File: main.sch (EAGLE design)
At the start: 4 parts

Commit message: Added initial components
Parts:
- added C1: 100n, resistor:C-EUC0805
- added C12, C2, C3, C4, C56, C62: 100nF, resistor:C-EUC0805
- added C5, C58, C61: 1uF_X5R, resistor:C-EUC0805
- added C57: 10nF X7R, resistor:C-EUC0805
- added C59, C60: 10uF, resistor:CPOL-EUSMCC
- added D1: BAT54S, diode:BAT54S
- added D14: BAT60JFILM, diode:DIODE-SOD323-W
- added IC17: LD398533RM, st-microelectronics:LD398533RM
- added IC18: LD1117S50TR, v-reg:LD117AS50TR
- added J1: DCJ0202, con-jack:DCJ0202
- added LED1, LED14: ROOD, led:LEDCHIP-LED0805
- added R1: 10K, resistor:R-EU_R0805
- added R2, R39, R6, R7, R8: 1K, resistor:R-EU_R0805
- added R3, R4, R5: 4K7, resistor:R-EU_R0805
- added S1: (no value), switch-omron:10-XX
- added U1: TMP275AIDR, TMP275AIDR:TMP275AIDR
- added U4: ESP-WROOM-32, esp32:ESP-WROOM-32
- added X1: 1751251, con-phoenix-350:1751251
- added X2: 87438-02, con-molex:87438-02
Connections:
- new net +12V: C59.+, IC18.IN, J1.1, X2-2.S
- new net +3V3: C12.1, C4.1, C5.1, C61.1, C62.1, D1.C2, IC17.VO, R1.2, R3.2, R4.2, R5.2, R7.2, R8.2, U1.V+, U4.3V3
- new net +5V: C60.+, D14.A, IC18.OUT, R39.2
- new net BTN: C2.1, R8.1, S1.S1
- new net GND: C1.2, C12.2, C2.2, C3.2, C4.2, C5.2, C56.2, C57.2, C58.2, C59.-, C60.-, C61.2, C62.2, D1.A1, IC17.GND, IC18.ADJ, J1.3, LED1.C, LED14.C, S1.P, U1.A0, U1.A1, U1.A2, U1.GND, U4.GND@1, U4.GND@15, U4.GND@38, X2-1.S
- new net I2C_SCL: R3.1, U1.SCL
- new net I2C_SDA: R4.1, U1.SDA
- new net LED: R6.2
- new net N$1: C1.1, D1.C1A2, R1.1, R2.2
- new net N$102: C57.1, IC17.BYPASS
- new net N$113: C56.1, C58.1, D14.C, IC17.VIN, IC17.VINH
- new net N$2: R2.1
- new net N$5: LED1.A, R6.1
- new net N$6: C3.1, R7.1, U4.EN
- new net N$99: LED14.A, R39.1
- new net RDX0: U4.RXD0
- new net TEMP_ALERT: R5.1, U1.ALERT
- new net TXD0: U4.TXD0

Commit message: Update :)
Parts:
- added C10, C7, C9: 100n, resistor:C-EUC0805
- added C6, C8: 10nF X7R, resistor:C-EUC0805
- added D2: BAT54S, diode:BAT54S
- added D3: BAT60JFILM, diode:DIODE-SOD323-W
- added IC1, IC2: PM8834-SO08N, PM8834:PM8834-SO08N
- added JP1: (no value), pinhead:PINHD-1X6
- added Q1, Q2, Q3, Q4: IRF3205SPBF, IRF3205SPBF:IRF3205SPBF
- added R10: 1K, resistor:R-EU_R0805
- added R11, R12, R13, R14, R9: 10K, resistor:R-EU_R0805
- added X3: 1751251, con-phoenix-350:1751251
- added X4: 1751277, con-phoenix-350:1751277
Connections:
- net N$1 renamed INP2
- new net CTS: JP1.6
- new net INP1: C10.1, D2.C1A2, R10.2, R9.1
- new net N$1: R11.2
- new net N$10: IC1.EN1, IC2.EN1, R11.1, R13.1
- new net N$12: IC1.OUT1, Q2.G
- new net N$13: IC1.OUT2, Q1.G
- new net N$14: Q2.D, X4-3.K
- new net N$15: IC2.OUT1, Q4.G
- new net N$16: IC2.OUT2, Q3.G
- new net N$17: Q3.D, X4-4.K
- new net N$18: Q4.D, X4-5.K
- new net N$19: R12.2
- new net N$20: R10.1, X3-2.K
- new net N$22: X3-1.K
- new net N$23: R14.2
- new net N$24: R13.2
- new net N$4: X1-1.K
- new net N$7: Q1.D, X4-2.K
- new net N$9: IC1.IN2, IC2.IN2
- new net PWM1: IC1.IN1
- new net PWM2: IC1.EN2, R12.1
- new net PWM3: IC2.IN1
- new net PWM4: IC2.EN2, R14.1
- new net RTS: JP1.5
- new net UART_5V: D3.A, JP1.1
- net +12V: now also C6.1, C7.1, C8.1, C9.1, IC1.VCC, IC2.VCC, X4-1.K
- net +3V3: now also D2.C2, R9.2
- net GND: now also C10.2, C6.2, C7.2, C8.2, C9.2, D2.A1, IC1.GND, IC2.GND, JP1.2, Q1.S, Q2.S, Q3.S, Q4.S, X1-3.K, X3-3.K
- net N$113: now also D3.C
- net N$2: now also X1-2.K
- net RDX0: now also JP1.4
- net TXD0: now also JP1.3
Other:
- note added: "RXD"
- note added: "TXD"

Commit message: layouting
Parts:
- removed X2: 87438-02, con-molex:87438-02
- added D4: TSOP57238TT1, SparkFun-Sensors:TSOP57238TT1
- added R15, R16: 1K, resistor:R-EU_R0805
- added U2: SI7021, SparkFun-Sensors:SI7021
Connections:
- removed net PWM4: IC2.EN2, R14.1
- new net PWM0: IC1.IN1, U4.IO18
- net +12V: no longer X2-2.S
- net GND: now also R15.1, R16.1; no longer X2-1.S
- net N$2: now also R15.2
- net N$20: now also R16.2
- net PWM1: now also IC1.EN2, R12.1, U4.IO19; no longer IC1.IN1
- net PWM2: now also IC2.IN1, U4.IO22; no longer IC1.EN2, R12.1
- net PWM3: now also IC2.EN2, R14.1, U4.IO23; no longer IC2.IN1
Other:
- moved on the sheet: X1-1, X1-2, X1-3, X3-1, X3-2, X3-3

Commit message: added level shifters
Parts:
- removed J1: DCJ0202, con-jack:DCJ0202
- added JP2: (no value), pinhead:PINHD-1X4
- added JP3, JP4, JP6: (no value), adafruit:PINHD-1X3
- added Q5, Q6, Q7, Q8: BSS138, SparkFun:MOSFET-NCHANNELSMD
- added R17, R18: 1K, resistor:R-EU_R0805
- added R19, R20, R21, R22, R23, R24, R25, R26, R27, R28, R29, R30: 10K, resistor:R-EU_R0805
- added X2: 1751248, con-phoenix-350:1751248
- JP1: device pinhead:PINHD-1X6 -> adafruit:PINHD-1X3
- R10, R2: value 1K -> 10R
- R15, R16: value 1K -> X
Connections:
- removed net CTS: JP1.6
- removed net N$1: R11.2
- removed net N$19: R12.2
- removed net N$23: R14.2
- removed net N$24: R13.2
- removed net RTS: JP1.5
- new net HV: JP1.1, JP3.1, JP4.1, JP6.1, R24.1, R26.1, R28.1, R30.1
- new net HV1: JP6.2, Q5.D, R24.2
- new net HV2: JP1.2, Q6.D, R26.2
- new net HV3: JP3.2, Q7.D, R28.2
- new net HV4: JP4.2, Q8.D, R30.2
- new net LV0: Q5.S, R23.2
- new net LV1: Q6.S, R25.2
- new net LV2: Q7.S, R27.2
- new net LV3: Q8.S, R29.2
- new net N$2001: IC2.IN2, R14.1
- new net N$2OO: IC2.EN1, R13.1
- new net N$3: D2.C1A2, R10.2, R17.1
- new net N$8: D1.C1A2, R18.1, R2.2
- net +12V: now also R11.2, R12.2, X2-1.K; no longer J1.1
- net +3V3: now also Q5.G, Q6.G, Q7.G, Q8.G, R23.1, R25.1, R27.1, R29.1
- net BTN: now also U4.IO34
- net GND: now also JP1.3, JP2.2, JP3.3, JP4.3, JP6.3, R13.2, R14.2, R19.2, R20.2, R21.2, R22.2, X2-2.K; no longer J1.3, JP1.2
- net I2C_SCL: now also R4.1, U4.IO22; no longer R3.1
- net I2C_SDA: now also R3.1, U4.IO23; no longer R4.1
- net INP1: now also R17.2, U4.IO25; no longer D2.C1A2, R10.2
- net INP2: now also R18.2, U4.IO33; no longer D1.C1A2, R2.2
- net LED: now also U4.IO32
- net N$10: no longer IC2.EN1, R13.1
- net N$9: now also R12.1; no longer IC2.IN2
- net PWM0: now also R22.1, U4.IO17; no longer U4.IO18
- net PWM1: now also R21.1, U4.IO5; no longer R12.1, U4.IO19
- net PWM2: now also R20.1, U4.IO18; no longer U4.IO22
- net PWM3: now also R19.1, U4.IO19; no longer R14.1, U4.IO23
- net RDX0: now also JP2.4; no longer JP1.4
- net TEMP_ALERT: now also U4.IO21
- net TXD0: now also JP2.3; no longer JP1.3
- net UART_5V: now also JP2.1; no longer JP1.1
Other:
- moved on the sheet: C1, C10, C8, C9, IC1, IC2, Q1, Q2, Q3, Q4, R1, R11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

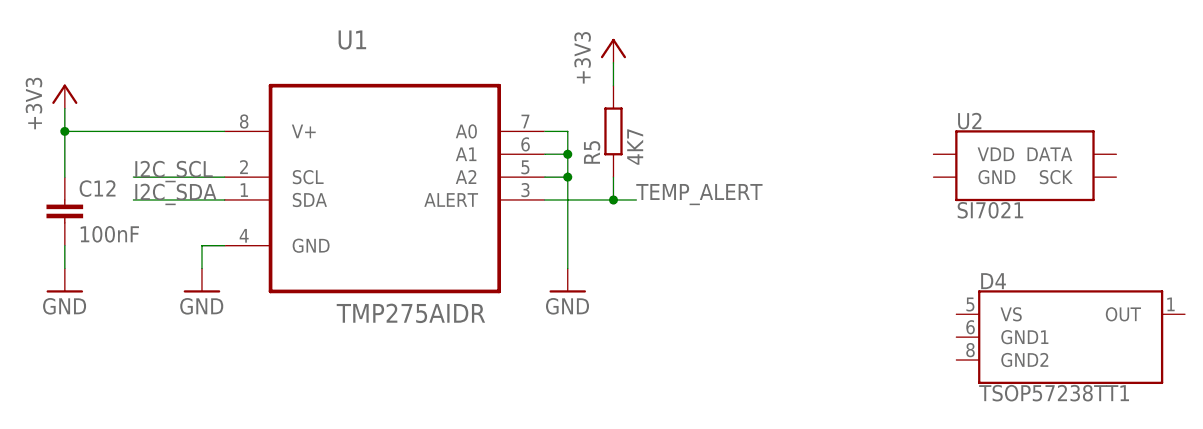
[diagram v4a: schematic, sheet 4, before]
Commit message: Removed sensors
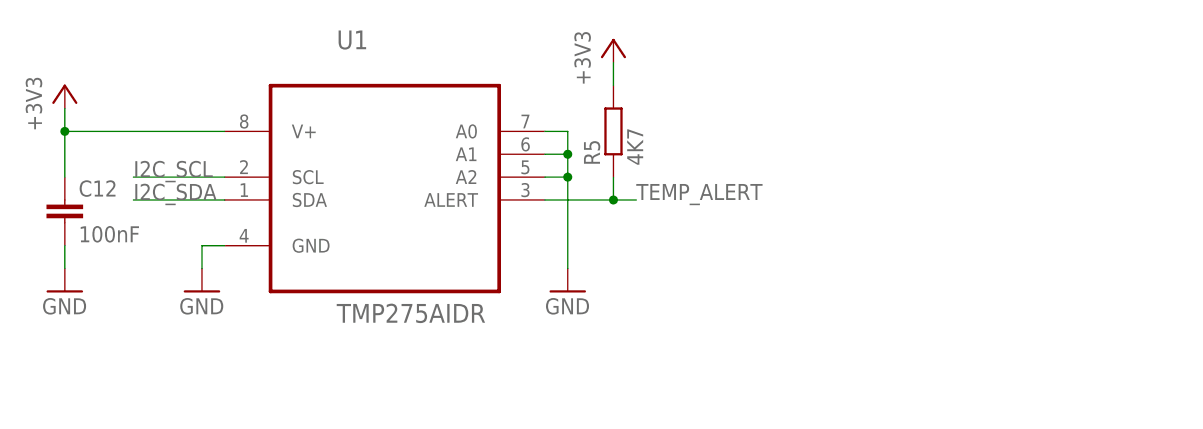
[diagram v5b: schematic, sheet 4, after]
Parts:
- removed D4: TSOP57238TT1, SparkFun-Sensors:TSOP57238TT1
- removed U2: SI7021, SparkFun-Sensors:SI7021
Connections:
- net +5V: now also JP6.1, R24.1
- net HV: no longer JP6.1, R24.1
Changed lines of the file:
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@@
 <part name="R16" library="resistor" library_urn="urn:adsk.eagle:library:348" deviceset="R-EU_" device="R0805" package3d_urn="urn:adsk.eagle:package:23553/2" value="X"/>
 <part name="GND31" library="supply1" library_urn="urn:adsk.eagle:library:371" deviceset="GND" device=""/>
-<part name="U2" library="SparkFun-Sensors" library_urn="urn:adsk.eagle:library:534" deviceset="SI7021" device="" package3d_urn="urn:adsk.eagle:package:39974/1"/>
-<part name="D4" library="SparkFun-Sensors" library_urn="urn:adsk.eagle:library:534" deviceset="TSOP57238TT1" device="" package3d_urn="urn:adsk.eagle:package:39958/1"/>
 <part name="R17" library="resistor" library_urn="urn:adsk.eagle:library:348" deviceset="R-EU_" device="R0805" package3d_urn="urn:adsk.eagle:package:23553/2" value="1K"/>
 <part name="R18" library="resistor" library_urn="urn:adsk.eagle:library:348" deviceset="R-EU_" device="R0805" package3d_urn="urn:adsk.eagle:package:23553/2" value="1K"/>
@@
 <part name="R23" library="resistor" library_urn="urn:adsk.eagle:library:348" deviceset="R-EU_" device="R0805" package3d_urn="urn:adsk.eagle:package:23553/2" value="10K"/>
 <part name="R24" library="resistor" library_urn="urn:adsk.eagle:library:348" deviceset="R-EU_" device="R0805" package3d_urn="urn:adsk.eagle:package:23553/2" value="10K"/>
-<part name="P+15" library="SparkFun" deviceset="VCC" device="" value="HV"/>
 <part name="+3V13" library="supply1" library_urn="urn:adsk.eagle:library:371" deviceset="+3V3" device=""/>
 <part name="GND37" library="supply1" library_urn="urn:adsk.eagle:library:371" deviceset="GND" device=""/>
@@
 <part name="P+12" library="SparkFun" deviceset="VCC" device="" value="HV"/>
 <part name="+3V16" library="supply1" library_urn="urn:adsk.eagle:library:371" deviceset="+3V3" device=""/>
+<part name="P+13" library="supply1" library_urn="urn:adsk.eagle:library:371" deviceset="+5V" device=""/>
 </parts>
 <sheets>
@@
 <attribute name="VALUE" x="189.738" y="-19.05" size="1.778" layer="96" rot="R270"/>
 </instance>
-<instance part="P+15" gate="1" x="193.04" y="-12.7" smashed="yes">
-<attribute name="VALUE" x="192.024" y="-9.144" size="1.778" layer="96"/>
-</instance>
 <instance part="+3V13" gate="G$1" x="177.8" y="-10.16" smashed="yes">
 <attribute name="VALUE" x="175.26" y="-15.24" size="1.778" layer="96" rot="R90"/>
@@
 <instance part="+3V16" gate="G$1" x="289.56" y="-10.16" smashed="yes">
 <attribute name="VALUE" x="287.02" y="-15.24" size="1.778" layer="96" rot="R90"/>
+</instance>
+<instance part="P+13" gate="1" x="193.04" y="-10.16" smashed="yes">
+<attribute name="VALUE" x="190.5" y="-15.24" size="1.778" layer="96" rot="R90"/>
 </instance>
 </instances>
@@
 <net name="HV" class="0">
 <segment>
-<wire x1="193.04" y1="-17.78" x2="193.04" y2="-15.24" width="0.1524" layer="91"/>
-<pinref part="R24" gate="G$1" pin="1"/>
-<pinref part="P+15" gate="1" pin="VCC"/>
-<pinref part="JP6" gate="A" pin="1"/>
-<wire x1="193.04" y1="-15.24" x2="193.04" y2="-12.7" width="0.1524" layer="91"/>
-<wire x1="203.2" y1="-27.94" x2="198.12" y2="-27.94" width="0.1524" layer="91"/>
-<wire x1="198.12" y1="-27.94" x2="198.12" y2="-15.24" width="0.1524" layer="91"/>
-<wire x1="198.12" y1="-15.24" x2="193.04" y2="-15.24" width="0.1524" layer="91"/>
-<junction x="193.04" y="-15.24"/>
-</segment>
-<segment>
 <wire x1="231.14" y1="-17.78" x2="231.14" y2="-15.24" width="0.1524" layer="91"/>
 <pinref part="R26" gate="G$1" pin="1"/>
@@
 <pinref part="R23" gate="G$1" pin="2"/>
 <label x="172.72" y="-30.48" size="1.778" layer="95"/>
+</segment>
+</net>
+<net name="+5V" class="0">
+<segment>
+<wire x1="193.04" y1="-17.78" x2="193.04" y2="-15.24" width="0.1524" layer="91"/>
+<pinref part="R24" gate="G$1" pin="1"/>
+<pinref part="JP6" gate="A" pin="1"/>
+<wire x1="203.2" y1="-27.94" x2="198.12" y2="-27.94" width="0.1524" layer="91"/>
+<wire x1="198.12" y1="-27.94" x2="198.12" y2="-15.24" width="0.1524" layer="91"/>
+<wire x1="198.12" y1="-15.24" x2="193.04" y2="-15.24" width="0.1524" layer="91"/>
+<pinref part="P+13" gate="1" pin="+5V"/>
+<wire x1="193.04" y1="-15.24" x2="193.04" y2="-12.7" width="0.1524" layer="91"/>
+<junction x="193.04" y="-15.24"/>
 </segment>
 </net>
@@
 <attribute name="VALUE" x="76.2" y="60.96" size="1.778" layer="96" rot="R90"/>
 </instance>
-<instance part="U2" gate="G$1" x="124.46" y="50.8" smashed="yes">
-<attribute name="NAME" x="116.84" y="56.134" size="1.778" layer="95" font="vector"/>
-<attribute name="VALUE" x="116.84" y="48.006" size="1.778" layer="96" font="vector" align="top-left"/>
-</instance>
-<instance part="D4" gate="G$1" x="129.54" y="33.02" smashed="yes">
-<attribute name="NAME" x="119.38" y="38.354" size="1.778" layer="95" font="vector"/>
-<attribute name="VALUE" x="119.38" y="27.686" size="1.778" layer="96" font="vector" align="top-left"/>
-</instance>
 </instances>

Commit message: P1 port and layouting
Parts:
- removed D3: BAT60JFILM, diode:DIODE-SOD323-W
- removed JP2: (no value), pinhead:PINHD-1X4
- removed LED1: ROOD, led:LEDCHIP-LED0805
- removed R6: 1K, resistor:R-EU_R0805
- added C11: (no value), resistor:CPOL-EUSMCA
- added C13, C30: 100nF, resistor:C-EUC0805
- added C14: 100n, resistor:C-EUC0805
- added C28, C29: 12pF, resistor:C-EUC0805
- added CN2: (no value), adafruit:USBMINIB
- added D4: BAT54S, diode:BAT54S
- added D5: BAT60JFILM, diode:DIODE-SOD323-W
- added IC4: CP2102, silabs:CP2102
- added J1: RJ11, SparkFun-Connectors:RJ11-6
- added JP5: (no value), pinhead:PINHD-1X6
- added LED2: RGBLED5050, adafruit:RGBLED5050
- added Q10: (no value), crystal:CRYSTALTC38H
- added Q11, Q12, Q9: BSS138, SparkFun:MOSFET-NCHANNELSMD
- added R31, R32: 0R, resistor:R-EU_R0805
- added R33: 2K, resistor:R-EU_R0805
- added R34, R40, R42, R43, R44, R45: 10K, resistor:R-EU_R0805
- added R35: 22K1, resistor:R-EU_R0805
- added R36: 47K5, resistor:R-EU_R0805
- added R37, R38: (no value), resistor:R-EU_R0805
- added R41: 1K, resistor:R-EU_R0805
- added S3: MOMENTARY-SWITCH-SPST-SMD-5.2-REDUNDANT, SparkFun-Switches:MOMENTARY-SWITCH-SPST-SMD-5.2-REDUNDANT
- added T1, T2, T3: SS8050-G, transistor:BCF29-NPN-SOT23-BEC
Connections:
- removed net N$113: C56.1, C58.1, D14.C, D3.C, IC17.VIN, IC17.VINH
- removed net N$5: LED1.A, R6.1
- removed net RDX0: JP2.4, U4.RXD0
- removed net UART_5V: D3.A, JP2.1
- new net CTS: IC4.CTS, JP5.6
- new net DCD: IC4.DCD
- new net DSR: IC4.DSR
- new net DTR: IC4.DTR, R42.1, T2.E
- new net EN: C3.1, R7.1, T1.C, U4.EN
- new net IO0: C30.1, S3.2, T2.C, U4.IO0
- new net N$1: Q9.D, R40.2
- new net N$11: LED2.GREEN_C, R44.1
- new net N$19: IC4.!SUSPEND, R34.1
- new net N$21: IC4.!RST, R33.1
- new net N$23: C60.+, D14.A, IC18.OUT, R39.2
- new net N$24: IC4.VBUS, R35.2, R36.2
- new net N$25: CN2.D-, IC4.D-
- new net N$26: J1.5, R37.1, R38.1
- new net N$27: C14.1, D4.C1A2, R38.2, T3.B
- new net N$28: R41.1, T3.C
- new net N$29: LED2.BLUE_C, R45.1
- new net N$30: LED2.RED_C, R40.1
- new net N$31: Q11.D, R44.2
- new net N$32: Q12.D, R45.2
- new net N$37: Q12.G
- new net N$38: C28.1, Q10.2, U4.IO32
- new net N$39: C29.1, Q10.1, U4.IO33
- new net N$40: Q11.G
- new net N$41: Q9.G
- new net N$42: R42.2, T1.B
- new net N$43: R43.2, T2.B
- new net RI: IC4.RI
- new net RTS: IC4.RTS, JP5.5, R43.1, T1.E
- new net RXD: IC4.RXD, JP5.3, R32.1
- new net RXD0: R31.2, U4.RXD0
- new net TXD: IC4.TXD, JP5.4, R31.1
- new net VBUS: CN2.VBUS, D5.A, JP5.1, R35.1
- net +3V3: now also C11.+, C13.1, IC4.REGIN, IC4.VDD, LED2.BLUE_A, LED2.GREEN_A, LED2.RED_A, R33.2, R41.2
- net +5V: now also C56.1, C58.1, D14.C, D4.C2, D5.C, IC17.VIN, IC17.VINH, J1.2, R37.2; no longer C60.+, D14.A, IC18.OUT, R39.2
- net BTN: now also S1.S; no longer S1.S1
- net GND: now also C11.-, C13.2, C14.2, C28.2, C29.2, C30.2, CN2.GND, D4.A1, IC4.GND, IC4.GND@EXP, IC4.GND@M, J1.3, JP5.2, Q11.S, Q12.S, Q9.S, R34.2, R36.1, S3.1, T3.E; no longer JP2.2, LED1.C
- net INP1: now also U4.IO26; no longer U4.IO25
- net INP2: now also U4.IO25; no longer U4.IO33
- net LED: now also U4.IO27; no longer R6.2, U4.IO32
- net N$6: now also CN2.D+, IC4.D+; no longer C3.1, R7.1, U4.EN
- net TXD0: now also R32.2; no longer JP2.3
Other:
- moved on the sheet: C2, C3, C4, C5, R7, R8, S1

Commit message: Updatesss
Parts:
- removed C7, C9: 100n, resistor:C-EUC0805
- removed JP5: (no value), pinhead:PINHD-1X6
- removed T3: SS8050-G, transistor:BCF29-NPN-SOT23-BEC
- removed X1, X3: 1751251, con-phoenix-350:1751251
- added C15: 100n, resistor:C-EUC0805
- added D3: BAT54S, diode:BAT54S
- added Q13: BSS138, SparkFun:MOSFET-NCHANNELSMD
- added R46: 10R, resistor:R-EU_R0805
- added R47: X, resistor:R-EU_R0805
- added R48: 1K, resistor:R-EU_R0805
- added R6: 10K, resistor:R-EU_R0805
- added X5: 1751280, con-phoenix-350:1751280
- C6, C8: value 10nF X7R -> 1uF X7R
- R37: value (none) -> 10K
- R38: value (none) -> 1K
- R41: value 1K -> 10K
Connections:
- new net N$33: D3.C1A2, R46.2, R48.1
- new net N$5: R46.1, R47.2
- net +12V: now also R13.2, R14.2; no longer C7.1, C9.1
- net +3V3: now also D3.C2, R6.2
- net CTS: no longer JP5.6
- net GND: now also C15.2, D3.A1, Q13.S, R47.1, X5-3.K, X5-6.K; no longer C7.2, C9.2, JP5.2, R13.2, R14.2, T3.E, X1-3.K, X3-3.K
- net INP2: now also C15.1, R48.2, R6.1
- net N$10: now also IC1.IN2; no longer IC1.EN1
- net N$2: now also X5-5.K; no longer X1-2.K
- net N$20: now also X5-2.K; no longer X3-2.K
- net N$22: now also X5-1.K; no longer X3-1.K
- net N$27: now also Q13.G; no longer T3.B
- net N$28: now also Q13.D; no longer T3.C
- net N$4: now also X5-4.K; no longer X1-1.K
- net N$9: now also IC1.EN1; no longer IC1.IN2
- net RTS: no longer JP5.5
- net RXD: no longer JP5.3
- net TXD: no longer JP5.4
- net VBUS: no longer JP5.1
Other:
- moved on the sheet: R11, R12, R13, R14
